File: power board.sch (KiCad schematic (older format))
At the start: 30 parts, among them J1 Conn_01x02_Female, J10 Conn_01x02_Female, J11 Conn_01x02_Female, J12 Conn_01x02_Female, J2 Conn_01x02_Female, J3 Conn_01x02_Female, J4 Conn_01x02_Female, J5 Conn_01x02_Female, J6 Conn_01x02_Female, J7 Conn_01x02_Female, J8 Conn_01x02_Female, J9 Conn_01x02_Female, Q1 STP160N3LL, U1 THL-25-2411

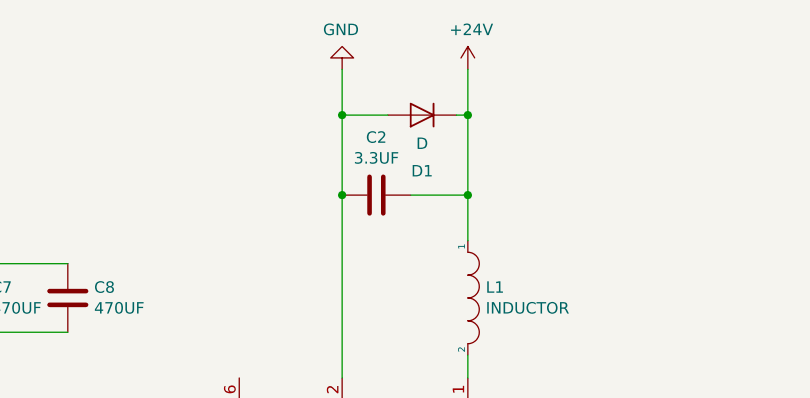
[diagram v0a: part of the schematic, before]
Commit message: deleted diode and added caps
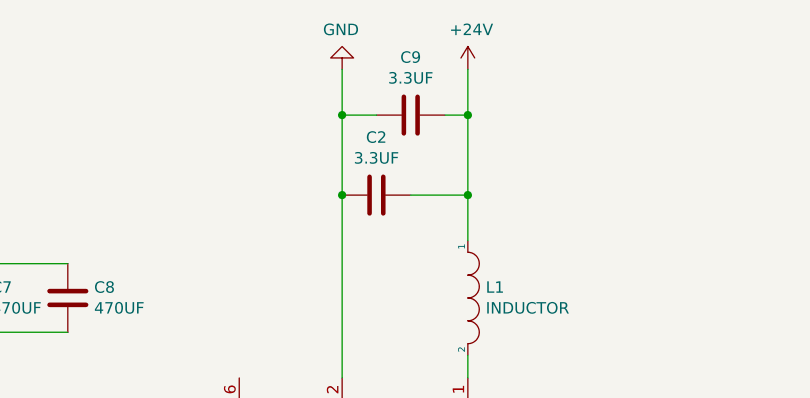
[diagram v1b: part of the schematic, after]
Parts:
- removed D1: D, symbol Device:D
- added C9: 3.3UF, Capacitor_SMD:C_0805_2012Metric_Pad1.15x1.40mm_HandSolder, symbol Device:C
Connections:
- net +24V: now also C9.2
- net GND: now also C9.1
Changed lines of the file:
@@
 EESchema Schematic File Version 4
+LIBS:power board-cache
 EELAYER 29 0
 EELAYER END
@@
 	1    0    0    1
 $EndComp
-$Comp
-L Device:D D1
-U 1 1 5CC0762E
-P 6200 1350
-F 0 "D1" H 6200 1566 50  0000 C BNN
-F 1 "D" H 6200 1475 50  0000 C CNN
-F 2 "" H 6200 1350 50  0001 C CNN
-F 3 "~" H 6200 1350 50  0001 C CNN
-	1    6200 1350
-	-1   0    0    1
-$EndComp
 Wire Wire Line
 	6150 1700 6400 1700
@@
 Wire Wire Line
 	6400 3950 6400 4350
-Wire Wire Line
-	6400 1150 6400 1350
 Connection ~ 6400 1700
-Wire Wire Line
-	6400 1350 6350 1350
-Connection ~ 6400 1350
-Wire Wire Line
-	6400 1350 6400 1700
-Wire Wire Line
-	6050 1350 5850 1350
-Wire Wire Line
-	5850 1350 5850 1150
-Wire Wire Line
-	5850 1350 5850 1700
-Connection ~ 5850 1350
-Connection ~ 5850 1700
 $Comp
 L power:GND #PWR0101
@@
 Connection ~ 1200 3750
 Connection ~ 1100 3750
+Wire Wire Line
+	6400 1150 6400 1350
+Connection ~ 5850 1700
+$Comp
+L Device:C C9
+U 1 1 5CB79BE5
+P 6150 1350
+F 0 "C9" V 6402 1350 50  0000 C CNN
+F 1 "3.3UF" V 6311 1350 50  0000 C CNN
+F 2 "Capacitor_SMD:C_0805_2012Metric_Pad1.15x1.40mm_HandSolder" H 6188 1200 50  0001 C CNN
+F 3 "~" H 6150 1350 50  0001 C CNN
+	1    6150 1350
+	0    -1   -1   0
+$EndComp
+Wire Wire Line
+	6300 1350 6400 1350
+Connection ~ 6400 1350
+Wire Wire Line
+	6400 1350 6400 1700
+Wire Wire Line
+	5850 1150 5850 1350
+Wire Wire Line
+	5850 1350 6000 1350
+Connection ~ 5850 1350
+Wire Wire Line
+	5850 1350 5850 1700
 $EndSCHEMATC

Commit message: final V1.0 sent out -gerbers zipped
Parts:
- added H1, H2, H3, H4: MountingHole, MountingHole:MountingHole_3.2mm_M3, symbol Mechanical:MountingHole
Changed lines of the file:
@@
 Wire Wire Line
 	5850 1350 5850 1700
+$Comp
+L Mechanical:MountingHole H1
+U 1 1 5CB9151C
+P 8250 4650
+F 0 "H1" H 8350 4696 50  0000 L CNN
+F 1 "MountingHole" H 8350 4605 50  0000 L CNN
+F 2 "MountingHole:MountingHole_3.2mm_M3" H 8250 4650 50  0001 C CNN
+F 3 "~" H 8250 4650 50  0001 C CNN
+	1    8250 4650
+	1    0    0    -1
+$EndComp
+$Comp
+L Mechanical:MountingHole H3
+U 1 1 5CB92ADC
+P 8850 4550
+F 0 "H3" H 8950 4596 50  0000 L CNN
+F 1 "MountingHole" H 8950 4505 50  0000 L CNN
+F 2 "MountingHole:MountingHole_3.2mm_M3" H 8850 4550 50  0001 C CNN
+F 3 "~" H 8850 4550 50  0001 C CNN
+	1    8850 4550
+	1    0    0    -1
+$EndComp
+$Comp
+L Mechanical:MountingHole H2
+U 1 1 5CB932AC
+P 8400 5050
+F 0 "H2" H 8500 5096 50  0000 L CNN
+F 1 "MountingHole" H 8500 5005 50  0000 L CNN
+F 2 "MountingHole:MountingHole_3.2mm_M3" H 8400 5050 50  0001 C CNN
+F 3 "~" H 8400 5050 50  0001 C CNN
+	1    8400 5050
+	1    0    0    -1
+$EndComp
+$Comp
+L Mechanical:MountingHole H4
+U 1 1 5CB935D1
+P 9100 5000
+F 0 "H4" H 9200 5046 50  0000 L CNN
+F 1 "MountingHole" H 9200 4955 50  0000 L CNN
+F 2 "MountingHole:MountingHole_3.2mm_M3" H 9100 5000 50  0001 C CNN
+F 3 "~" H 9100 5000 50  0001 C CNN
+	1    9100 5000
+	1    0    0    -1
+$EndComp
 $EndSCHEMATC

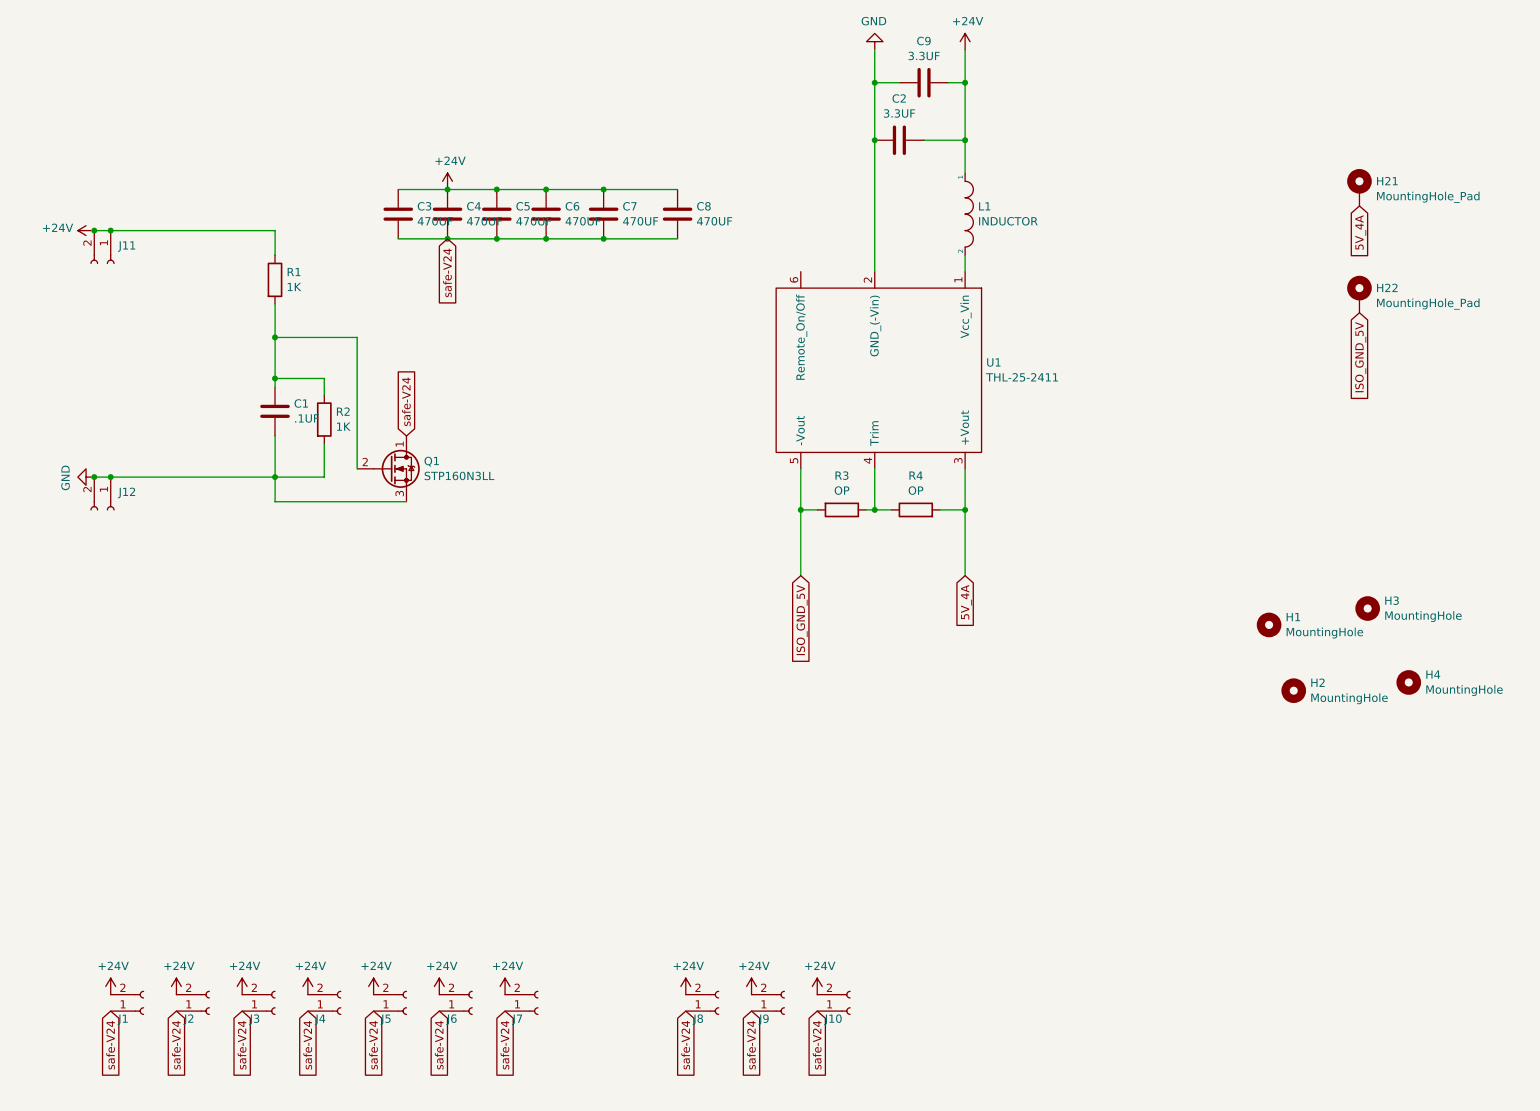
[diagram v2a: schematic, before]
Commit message: added leds annd switch and decreased size
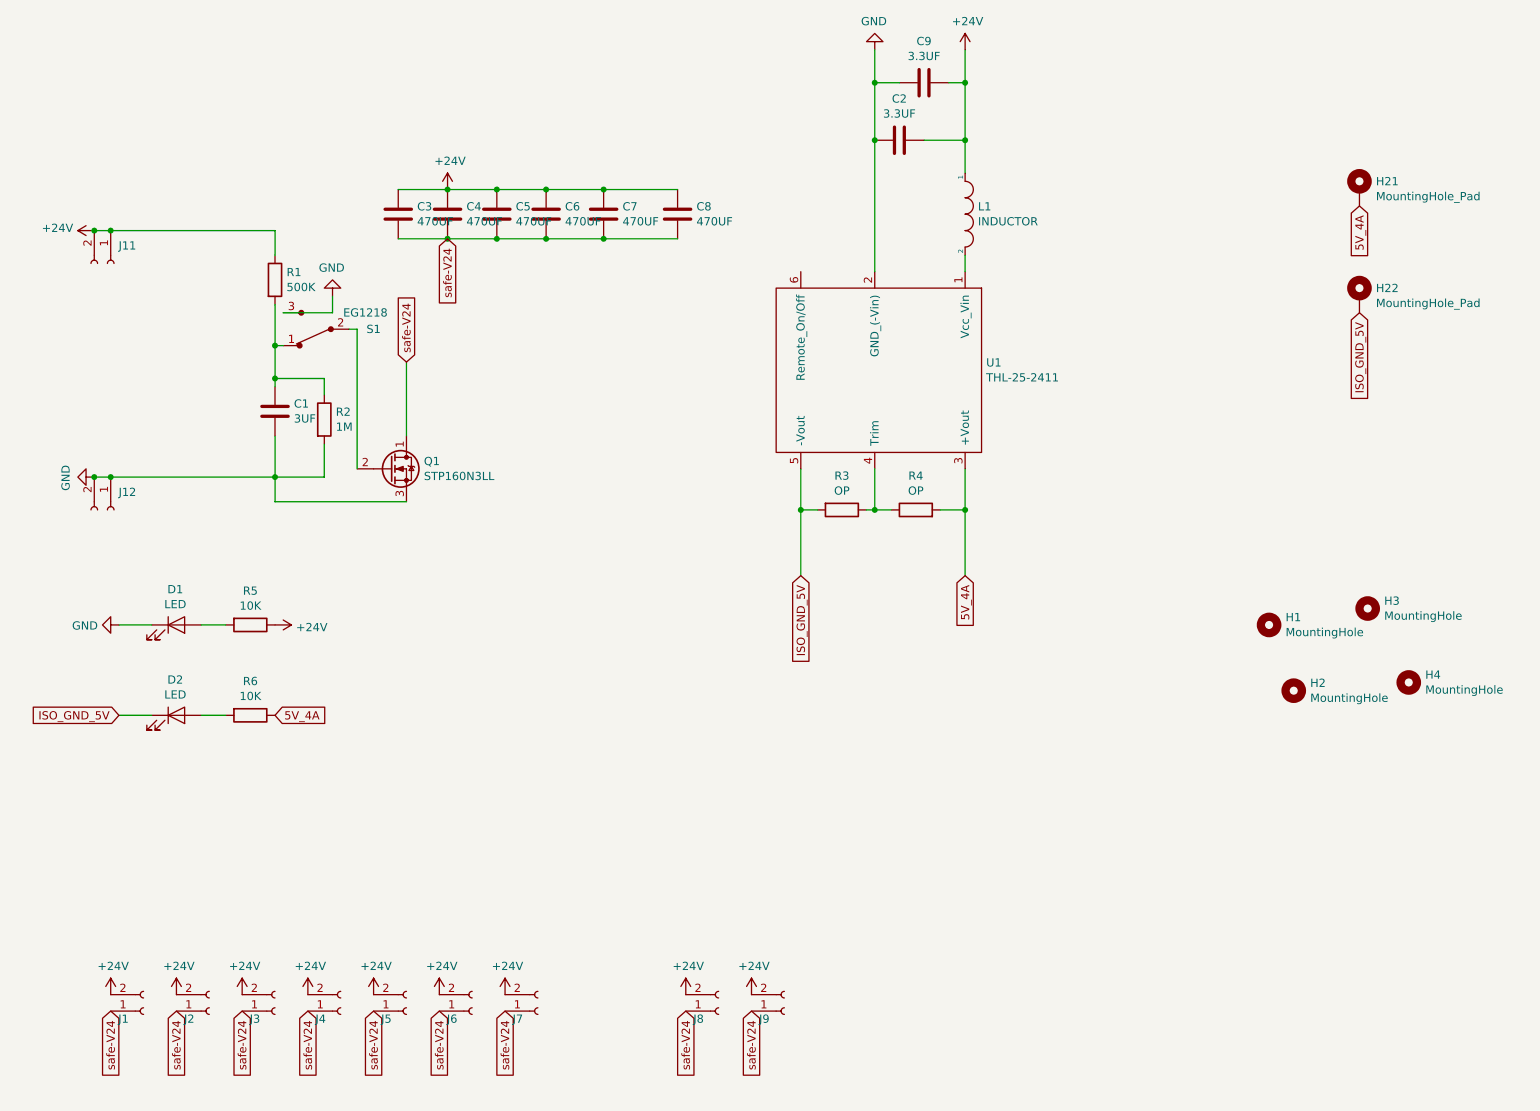
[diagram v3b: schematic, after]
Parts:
- removed J10: Conn_01x02_Female, RC-Battery-Connectors:XT-60_female, symbol Connector:Conn_01x02_Female
- added D1, D2: LED, LED_SMD:LED_0603_1608Metric_Pad1.05x0.95mm_HandSolder, symbol Device:LED
- added R5, R6: 10K, Resistor_SMD:R_0805_2012Metric_Pad1.15x1.40mm_HandSolder, symbol Device:R
- added S1: EG1218, digikey-footprints:Switch_Slide_11.6x4mm_EG1218, symbol dk_Slide-Switches:EG1218
- C1: value .1UF -> 3UF
- R1: value 1K -> 500K
- R2: value 1K -> 1M
- U1: footprint Converter_DCDC:Converter_DCDC_TRACO_TEN20-xxxx_THT -> Converter_DCDC:Converter_DCDC_TRACO_TEN20-xxxx_THT-modified
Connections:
- net +24V: now also R5.1
- net 5V_4A: now also R6.1
- net GND: now also D1.1 (K), S1.3
- net ISO_GND_5V: now also D2.1 (K)
- net at C1.1, R1.2, R2.1: now also S1.1; no longer Q1.2 (G)
- new net: Q1.2 (G), S1.2
- new net: D1.2 (A), R5.2
- new net: D2.2 (A), R6.2
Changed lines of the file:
@@
 P 2200 3350
 F 0 "C1" H 2315 3396 50  0000 L CNN
-F 1 ".1UF" H 2315 3305 50  0000 L CNN
+F 1 "3UF" H 2315 3305 50  0000 L CNN
 F 2 "Capacitor_SMD:C_0805_2012Metric_Pad1.15x1.40mm_HandSolder" H 2238 3200 50  0001 C CNN
 F 3 "~" H 2200 3350 50  0001 C CNN
@@
 F 0 "U1" H 6528 3546 50  0000 L CNN
 F 1 "THL-25-2411" H 6528 3455 50  0000 L CNN
-F 2 "Converter_DCDC:Converter_DCDC_TRACO_TEN20-xxxx_THT" H 5900 3300 50  0001 C CNN
+F 2 "Converter_DCDC:Converter_DCDC_TRACO_TEN20-xxxx_THT-modified" H 5900 3300 50  0001 C CNN
 F 3 "" H 5900 3300 50  0001 C CNN
 	1    5900 3300
@@
 P 2500 3400
 F 0 "R2" H 2570 3446 50  0000 L CNN
-F 1 "1K" H 2570 3355 50  0000 L CNN
+F 1 "1M" H 2570 3355 50  0000 L CNN
 F 2 "Resistor_SMD:R_0805_2012Metric_Pad1.15x1.40mm_HandSolder" V 2430 3400 50  0001 C CNN
 F 3 "~" H 2500 3400 50  0001 C CNN
@@
 P 2200 2550
 F 0 "R1" H 2270 2596 50  0000 L CNN
-F 1 "1K" H 2270 2505 50  0000 L CNN
+F 1 "500K" H 2270 2505 50  0000 L CNN
 F 2 "Resistor_SMD:R_0805_2012Metric_Pad1.15x1.40mm_HandSolder" V 2130 2550 50  0001 C CNN
 F 3 "~" H 2200 2550 50  0001 C CNN
@@
 	2500 3150 2200 3150
 Connection ~ 2200 3150
-Wire Wire Line
-	2200 3150 2200 2900
-Wire Wire Line
-	2700 3700 2700 2900
-Wire Wire Line
-	2700 2900 2200 2900
-Connection ~ 2200 2900
-Wire Wire Line
-	2200 2900 2200 2700
 Wire Wire Line
 	1200 3750 2200 3750
@@
 Wire Wire Line
 	2200 2400 2200 2250
-Text GLabel 3000 3500 1    50   Input ~ 0
+Text GLabel 3000 3050 1    50   Input ~ 0
 safe-V24
 Text GLabel 1200 7000 3    50   Input ~ 0
@@
 	1    0    0    1
 $EndComp
-Text GLabel 5500 7000 3    50   Input ~ 0
-safe-V24
-$Comp
-L power:+24V #PWR0112
-U 1 1 5CC2C495
-P 5500 6900
-F 0 "#PWR0112" H 5500 6750 50  0001 C CNN
-F 1 "+24V" H 5515 7073 50  0000 C CNN
-F 2 "" H 5500 6900 50  0001 C CNN
-F 3 "" H 5500 6900 50  0001 C CNN
-	1    5500 6900
-	1    0    0    -1
-$EndComp
-$Comp
-L Connector:Conn_01x02_Female J10
-U 1 1 5CC2C49B
-P 5700 7000
-F 0 "J10" H 5546 7048 50  0000 L CNN
-F 1 "Conn_01x02_Female" V 5637 7048 50  0001 R BNN
-F 2 "RC-Battery-Connectors:XT-60_female" H 5700 7000 50  0001 C CNN
-F 3 "~" H 5700 7000 50  0001 C CNN
-	1    5700 7000
-	1    0    0    1
-$EndComp
 Wire Wire Line
 	5400 3950 5400 4350
@@
 	1    0    0    -1
 $EndComp
+$Comp
+L Device:LED D1
+U 1 1 5CB97C20
+P 1600 4650
+F 0 "D1" H 1593 4866 50  0000 C CNN
+F 1 "LED" H 1593 4775 50  0000 C CNN
+F 2 "LED_SMD:LED_0603_1608Metric_Pad1.05x0.95mm_HandSolder" H 1600 4650 50  0001 C CNN
+F 3 "~" H 1600 4650 50  0001 C CNN
+	1    1600 4650
+	1    0    0    -1
+$EndComp
+$Comp
+L power:GND #PWR0114
+U 1 1 5CB988C7
+P 1250 4650
+F 0 "#PWR0114" H 1250 4400 50  0001 C CNN
+F 1 "GND" V 1255 4522 50  0000 R CNN
+F 2 "" H 1250 4650 50  0001 C CNN
+F 3 "" H 1250 4650 50  0001 C CNN
+	1    1250 4650
+	0    1    1    0
+$EndComp
+$Comp
+L Device:R R5
+U 1 1 5CB99204
+P 2050 4650
+F 0 "R5" V 1843 4650 50  0000 C CNN
+F 1 "10K" V 1934 4650 50  0000 C CNN
+F 2 "Resistor_SMD:R_0805_2012Metric_Pad1.15x1.40mm_HandSolder" V 1980 4650 50  0001 C CNN
+F 3 "~" H 2050 4650 50  0001 C CNN
+	1    2050 4650
+	0    1    1    0
+$EndComp
+Wire Wire Line
+	1900 4650 1750 4650
+$Comp
+L power:+24V #PWR0115
+U 1 1 5CB9A4FD
+P 2200 4650
+F 0 "#PWR0115" H 2200 4500 50  0001 C CNN
+F 1 "+24V" V 2215 4778 50  0000 L CNN
+F 2 "" H 2200 4650 50  0001 C CNN
+F 3 "" H 2200 4650 50  0001 C CNN
+	1    2200 4650
+	0    1    1    0
+$EndComp
+Wire Wire Line
+	1450 4650 1250 4650
+Wire Wire Line
+	2200 2700 2200 2950
+$Comp
+L dk_Slide-Switches:EG1218 S1
+U 1 1 5CC0385E
+P 2450 2850
+F 0 "S1" H 2100 2850 50  0000 C CNN
+F 1 "EG1218" H 2150 2750 50  0000 C CNN
+F 2 "digikey-footprints:Switch_Slide_11.6x4mm_EG1218" H 2650 3050 50  0001 L CNN
+F 3 "http://spec_sheets.e-switch.com/specs/P040040.pdf" H 2650 3150 60  0001 L CNN
+F 4 "EG1903-ND" H 2650 3250 60  0001 L CNN "Digi-Key_PN"
+F 5 "EG1218" H 2650 3350 60  0001 L CNN "MPN"
+F 6 "Switches" H 2650 3450 60  0001 L CNN "Category"
+F 7 "Slide Switches" H 2650 3550 60  0001 L CNN "Family"
+F 8 "http://spec_sheets.e-switch.com/specs/P040040.pdf" H 2650 3650 60  0001 L CNN "DK_Datasheet_Link"
+F 9 "/product-detail/en/e-switch/EG1218/EG1903-ND/101726" H 2650 3750 60  0001 L CNN "DK_Detail_Page"
+F 10 "SWITCH SLIDE SPDT 200MA 30V" H 2650 3850 60  0001 L CNN "Description"
+F 11 "E-Switch" H 2650 3950 60  0001 L CNN "Manufacturer"
+F 12 "Active" H 2650 4050 60  0001 L CNN "Status"
+	1    2450 2850
+	-1   0    0    1
+$EndComp
+Wire Wire Line
+	2250 2950 2200 2950
+Connection ~ 2200 2950
+Wire Wire Line
+	2200 2950 2200 3150
+$Comp
+L power:GND #PWR0116
+U 1 1 5CC0A55C
+P 2550 2650
+F 0 "#PWR0116" H 2550 2400 50  0001 C CNN
+F 1 "GND" H 2555 2477 50  0000 C CNN
+F 2 "" H 2550 2650 50  0001 C CNN
+F 3 "" H 2550 2650 50  0001 C CNN
+	1    2550 2650
+	-1   0    0    1
+$EndComp
+Wire Wire Line
+	2250 2750 2550 2750
+Wire Wire Line
+	2550 2750 2550 2650
+Wire Wire Line
+	2700 2850 2650 2850
+Wire Wire Line
+	2700 2850 2700 3700
+Wire Wire Line
+	3000 3050 3000 3500
+$Comp
+L Device:LED D2
+U 1 1 5CC1AA45
+P 1600 5200
+F 0 "D2" H 1593 5416 50  0000 C CNN
+F 1 "LED" H 1593 5325 50  0000 C CNN
+F 2 "LED_SMD:LED_0603_1608Metric_Pad1.05x0.95mm_HandSolder" H 1600 5200 50  0001 C CNN
+F 3 "~" H 1600 5200 50  0001 C CNN
+	1    1600 5200
+	1    0    0    -1
+$EndComp
+$Comp
+L Device:R R6
+U 1 1 5CC1AA51
+P 2050 5200
+F 0 "R6" V 1843 5200 50  0000 C CNN
+F 1 "10K" V 1934 5200 50  0000 C CNN
+F 2 "Resistor_SMD:R_0805_2012Metric_Pad1.15x1.40mm_HandSolder" V 1980 5200 50  0001 C CNN
+F 3 "~" H 2050 5200 50  0001 C CNN
+	1    2050 5200
+	0    1    1    0
+$EndComp
+Wire Wire Line
+	1900 5200 1750 5200
+Wire Wire Line
+	1450 5200 1250 5200
+Text GLabel 1250 5200 0    50   Input ~ 0
+ISO_GND_5V
+Text GLabel 2200 5200 2    50   Input ~ 0
+5V_4A
 $EndSCHEMATC
